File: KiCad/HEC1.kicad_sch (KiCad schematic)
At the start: 50 parts, among them J1 Barrel_Jack_Switch, J10 Conn_02x05_Odd_Even, J5 Screw_Terminal_01x02, K1 FINDER-34.51, SW2 SW_Push, U45 74LS14, U46 74LS123, U47 74LS74

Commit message: Finish protection overhaul
Disable ram chip select when page is marked as not present, change write protect to 1 as write enabled, 0 as disabled. Change XE interrupt timings.
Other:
- sheet HEC_Memory ports: added ATTR_P, SYS; removed ATTR_RI
- sheet HEC_Protection ports: added ATTR_P; removed ATTR_RI
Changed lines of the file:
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@@
   (junction (at 127 25.4) (diameter 0) (color 0 0 0 0)
+  )
+  (junction (at 171.45 60.96) (diameter 0) (color 0 0 0 0)
   )
   (junction (at 134.62 123.825) (diameter 0) (color 0 0 0 0)
@@
     (stroke (width 0) (type default))
   )
+  (wire (pts (xy 191.135 60.96) (xy 171.45 60.96))
+    (stroke (width 0) (type default))
+  )
   (wire (pts (xy 229.235 43.18) (xy 231.775 43.18))
     (stroke (width 0) (type default))
@@
     (stroke (width 0) (type default))
   )
-  (wire (pts (xy 171.45 47.625) (xy 171.45 66.675))
+  (wire (pts (xy 171.45 60.96) (xy 171.45 66.675))
+    (stroke (width 0) (type default))
+  )
+  (wire (pts (xy 171.45 47.625) (xy 171.45 60.96))
     (stroke (width 0) (type default))
   )
@@
       (effects (font (size 1.27 1.27)) (justify left))
     )
-    (pin "ATTR_RI" input (at 177.8 87.63 0)
-      (effects (font (size 1.27 1.27)) (justify right))
-    )
     (pin "ATTR_XE" input (at 177.8 90.17 0)
       (effects (font (size 1.27 1.27)) (justify right))
@@
     )
     (pin "RESET" input (at 177.8 99.06 0)
+      (effects (font (size 1.27 1.27)) (justify right))
+    )
+    (pin "ATTR_P" input (at 177.8 87.63 0)
       (effects (font (size 1.27 1.27)) (justify right))
     )
@@
       (effects (font (size 1.27 1.27)) (justify left))
     )
-    (pin "ATTR_RI" output (at 191.135 87.63 180)
-      (effects (font (size 1.27 1.27)) (justify left))
-    )
+    (pin "ATTR_P" output (at 191.135 87.63 180)
+      (effects (font (size 1.27 1.27)) (justify left))
+    )
+    (pin "SYS" input (at 191.135 60.96 180)
+      (effects (font (size 1.27 1.27)) (justify left))
+    )

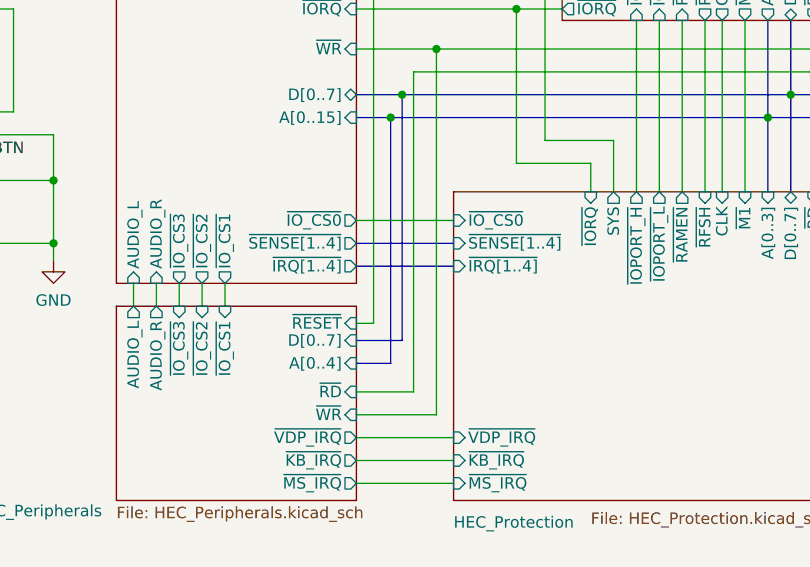
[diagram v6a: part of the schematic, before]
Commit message: Add I2C bus
Change audio pins on the bus to carry I2C signal. This can be used for configuring onboard devices such as RGB to HDMI converters, sound mixers, GPIOs, etc.
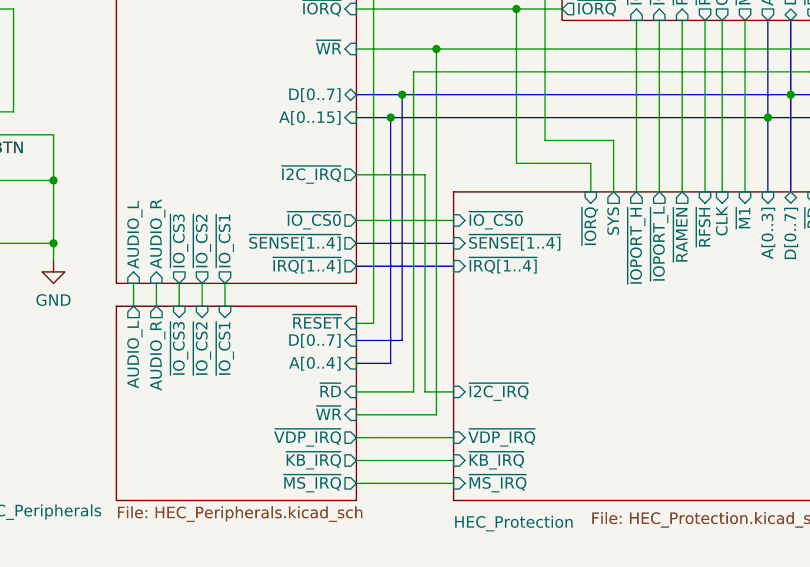
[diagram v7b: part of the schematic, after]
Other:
- sheet HEC_IO ports: added ~{I2C_IRQ}; removed none
- sheet HEC_Protection ports: added ~{I2C_IRQ}; removed none
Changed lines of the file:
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@@
+    (stroke (width 0) (type default))
+  )
+  (wire (pts (xy 120.65 64.77) (xy 120.65 88.9))
     (stroke (width 0) (type default))
   )
@@
     (stroke (width 0) (type default))
   )
+  (wire (pts (xy 113.03 64.77) (xy 120.65 64.77))
+    (stroke (width 0) (type default))
+  )
   (wire (pts (xy 116.84 123.825) (xy 125.73 123.825))
     (stroke (width 0) (type default))
@@
   )
   (bus (pts (xy 161.29 55.88) (xy 161.29 66.675))
+    (stroke (width 0) (type default))
+  )
+  (wire (pts (xy 120.65 88.9) (xy 123.825 88.9))
     (stroke (width 0) (type default))
   )
@@
       (effects (font (size 1.27 1.27)) (justify right))
     )
+    (pin "~{I2C_IRQ}" input (at 123.825 88.9 180)
+      (effects (font (size 1.27 1.27)) (justify left))
+    )
     (instances
       (project "HEC1"
@@
       (effects (font (size 1.27 1.27)) (justify right))
     )
+    (pin "~{I2C_IRQ}" output (at 113.03 64.77 0)
+      (effects (font (size 1.27 1.27)) (justify right))
+    )

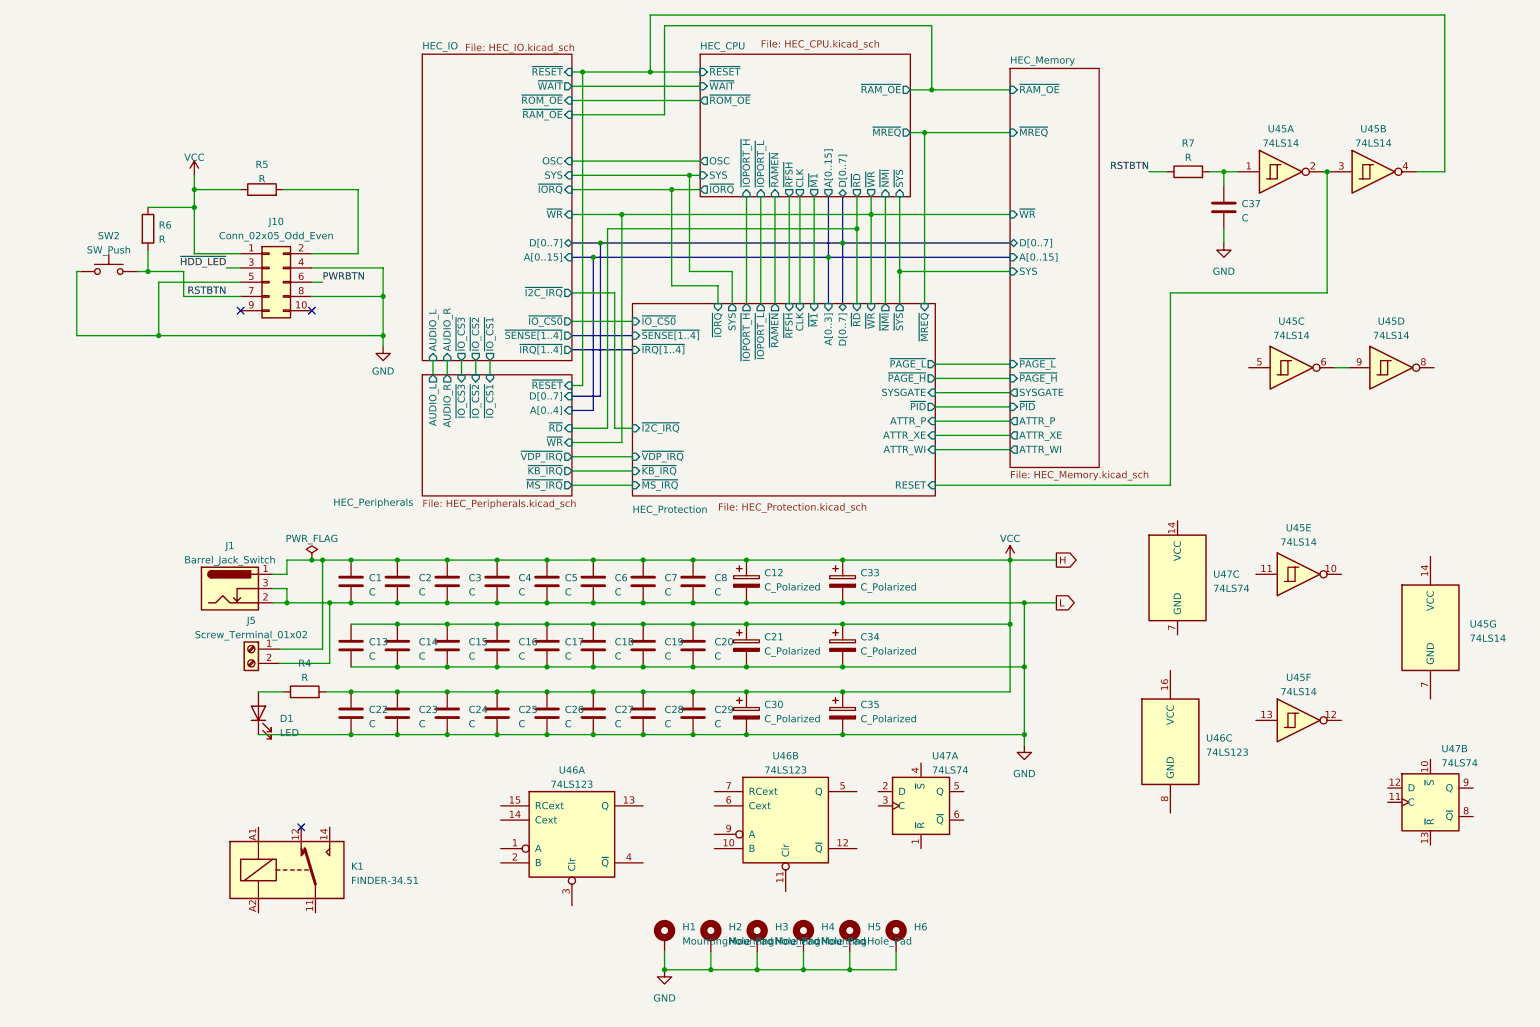
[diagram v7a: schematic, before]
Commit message: Fancy power circuit
Added a circuit to switch power, short press to power on, long press to power off.
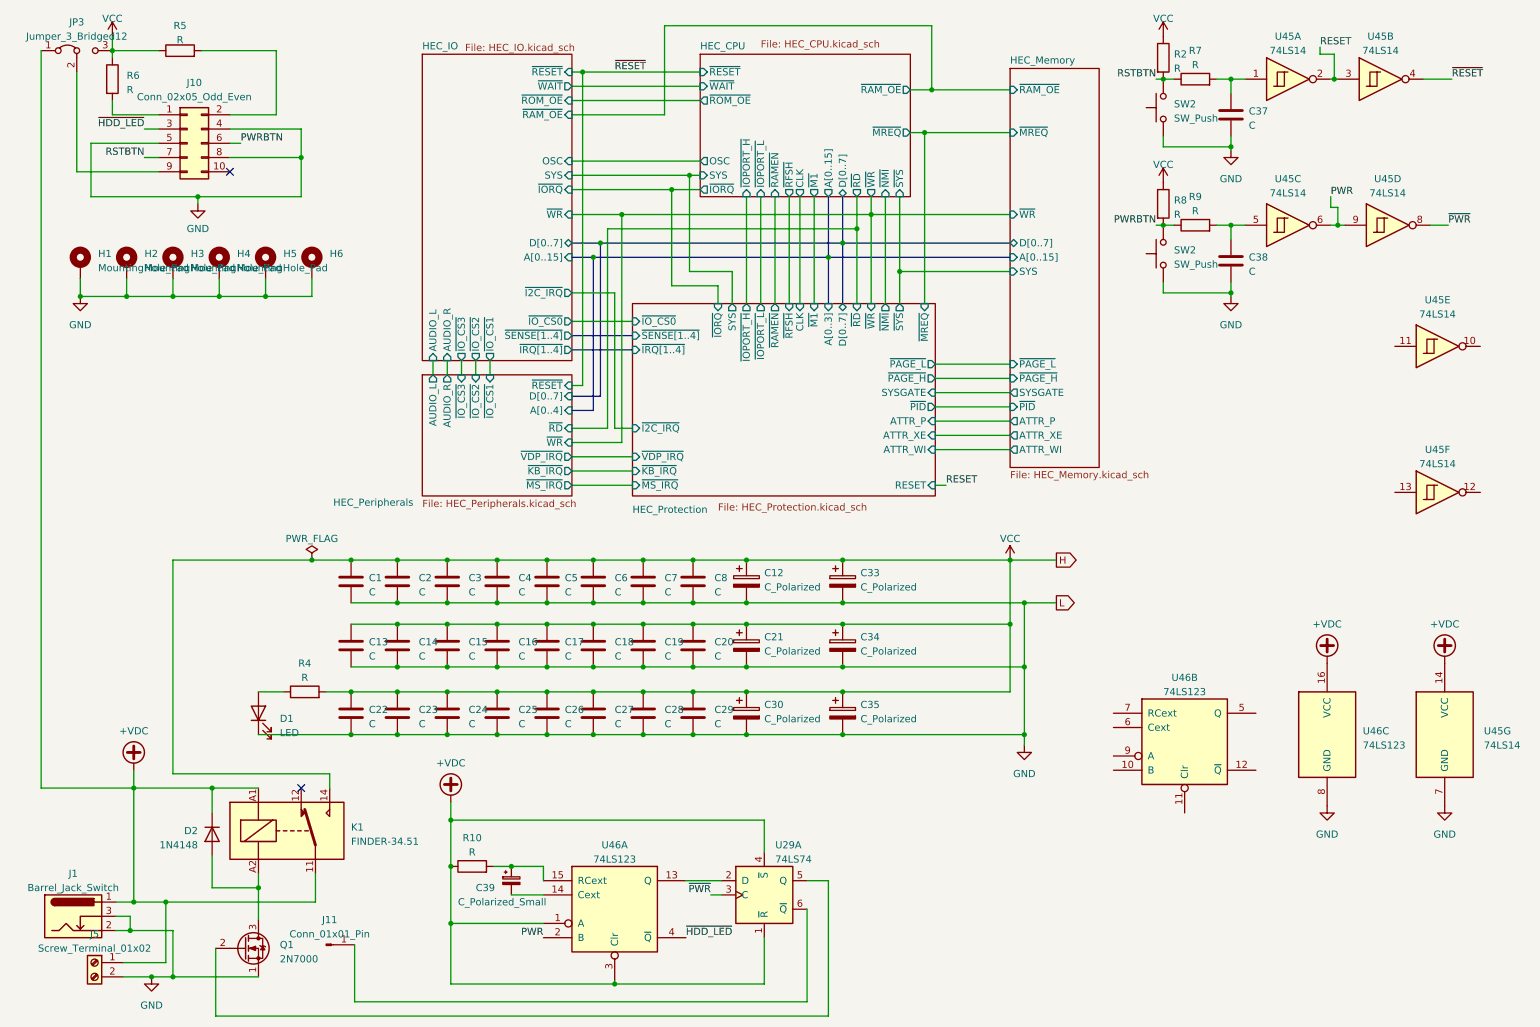
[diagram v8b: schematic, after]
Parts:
- removed SW2: SW_Push, Button_Switch_THT:SW_PUSH_6mm, symbol Switch:SW_Push
- removed U47: 74LS74, symbol 74xx:74LS74
- added C38: C, symbol Device:C
- added C39: C_Polarized_Small, symbol Device:C_Polarized_Small
- added D2: 1N4148, Diode_THT:D_DO-35_SOD27_P7.62mm_Horizontal, symbol Diode:1N4148
- added J11: Conn_01x01_Pin, Connector_PinHeader_2.54mm:PinHeader_1x01_P2.54mm_Vertical, symbol Connector:Conn_01x01_Pin
- added JP3: Jumper_3_Bridged12, symbol Jumper:Jumper_3_Bridged12
- added Q1: 2N7000, Package_TO_SOT_THT:TO-92_Inline, symbol Transistor_FET:2N7000
- added R10, R2, R8, R9: R, symbol Device:R
- added SW2 (x2): SW_Push, Button_Switch_THT:SW_PUSH_6mm, symbol Switch:SW_Push
- added U29: 74LS74, Library:DIP-14_W7.62mm_Socket_ThinPads, symbol 74xx:74LS74
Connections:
- net GND: now also U45.7 (GND), U46.8 (GND), C38.2, Q1.1 (S), SW2.2, SW2.2
- net PWRBTN: now also R8.2, R9.1, SW2.1
- net RSTBTN: now also R2.2, SW2.1; no longer R6.2
- net VCC: now also K1.14, JP3.3 (B), R2.1, R8.1; no longer J1.1, J10.1 (Pin_1), J5.1 (Pin_1)
- net ~{HDD_LED}: now also U46.4 (~{Q})
- net +VDC: now reaches U46.1 (A)
- net +VDC: now also J1.1, J5.1 (Pin_1), K1.11, K1.A1, U45.14 (VCC), U46.16 (VCC), U46.3 (Clr), D2.1 (K), JP3.1 (A), R10.1, U29.1 (~{R}), U29.4 (~{S})
- net at U46.13 (Q): now also U29.2 (D)
- net at U46.14 (Cext): now also C39.2
- net at U46.15 (RCext): now also C39.1, R10.2
- net PWR: now reaches U46.2 (B)
- net PWR: now also U45.6, U45.9
- net at K1.A2: now also D2.2 (A), Q1.3 (D)
- net at U45.5: now also C38.1, R9.2
- net ~{PWR}: now reaches U45.8
- net ~{PWR}: now also U29.3 (C)
- net at J10.9 (Pin_9): now also JP3.2 (C)
- net HEC_CPU/~{RESET} renamed ~{RESET}
- net HEC_Protection/RESET renamed RESET
- new net: J11.1 (Pin_1), U29.6 (~{Q})
- new net: Q1.2 (G), U29.5 (Q)
- new net: J10.1 (Pin_1), R6.2
- no-connect marks 3 -> 2
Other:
- moved on the sheet: C37, H1, H2, H3, H4, H5, H6, J1, J10, J5, K1, R5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
